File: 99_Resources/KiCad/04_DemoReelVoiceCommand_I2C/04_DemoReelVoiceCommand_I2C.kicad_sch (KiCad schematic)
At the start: 11 parts, among them J1 Conn_01x03_Pin, J4 Conn_01x03_Socket, M1 SEN0539_VoiceCommand, U1 BlueToothAudioR

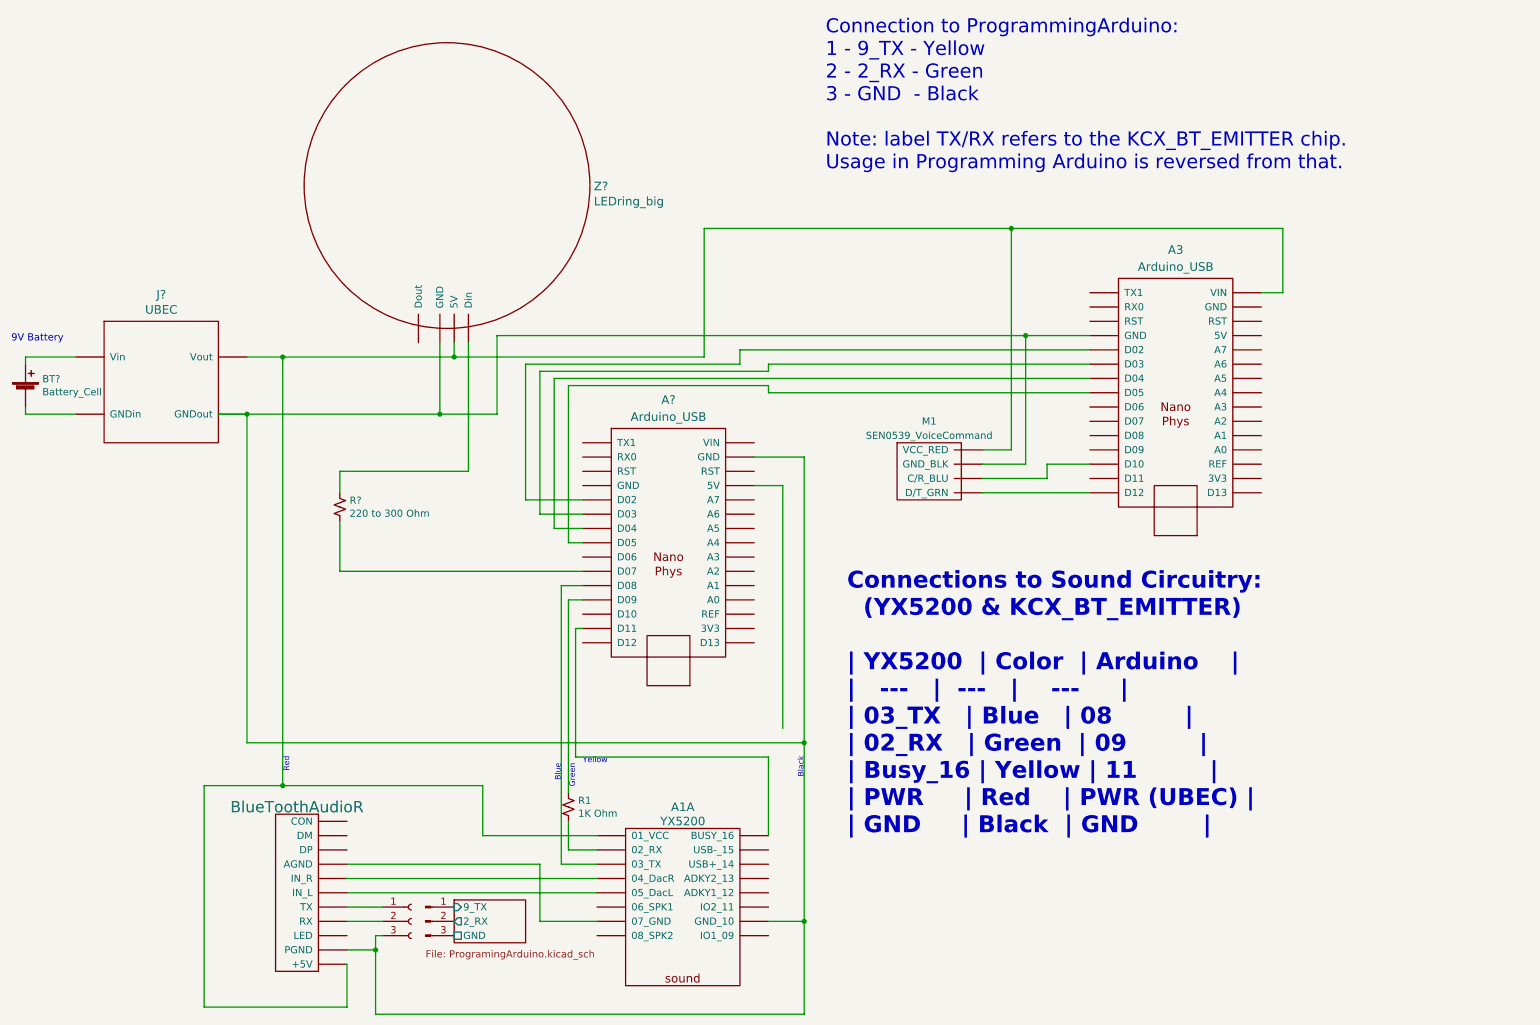
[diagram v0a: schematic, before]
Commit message: updates to UART and I2C versions of KiCad DemoReelVoiceCommand
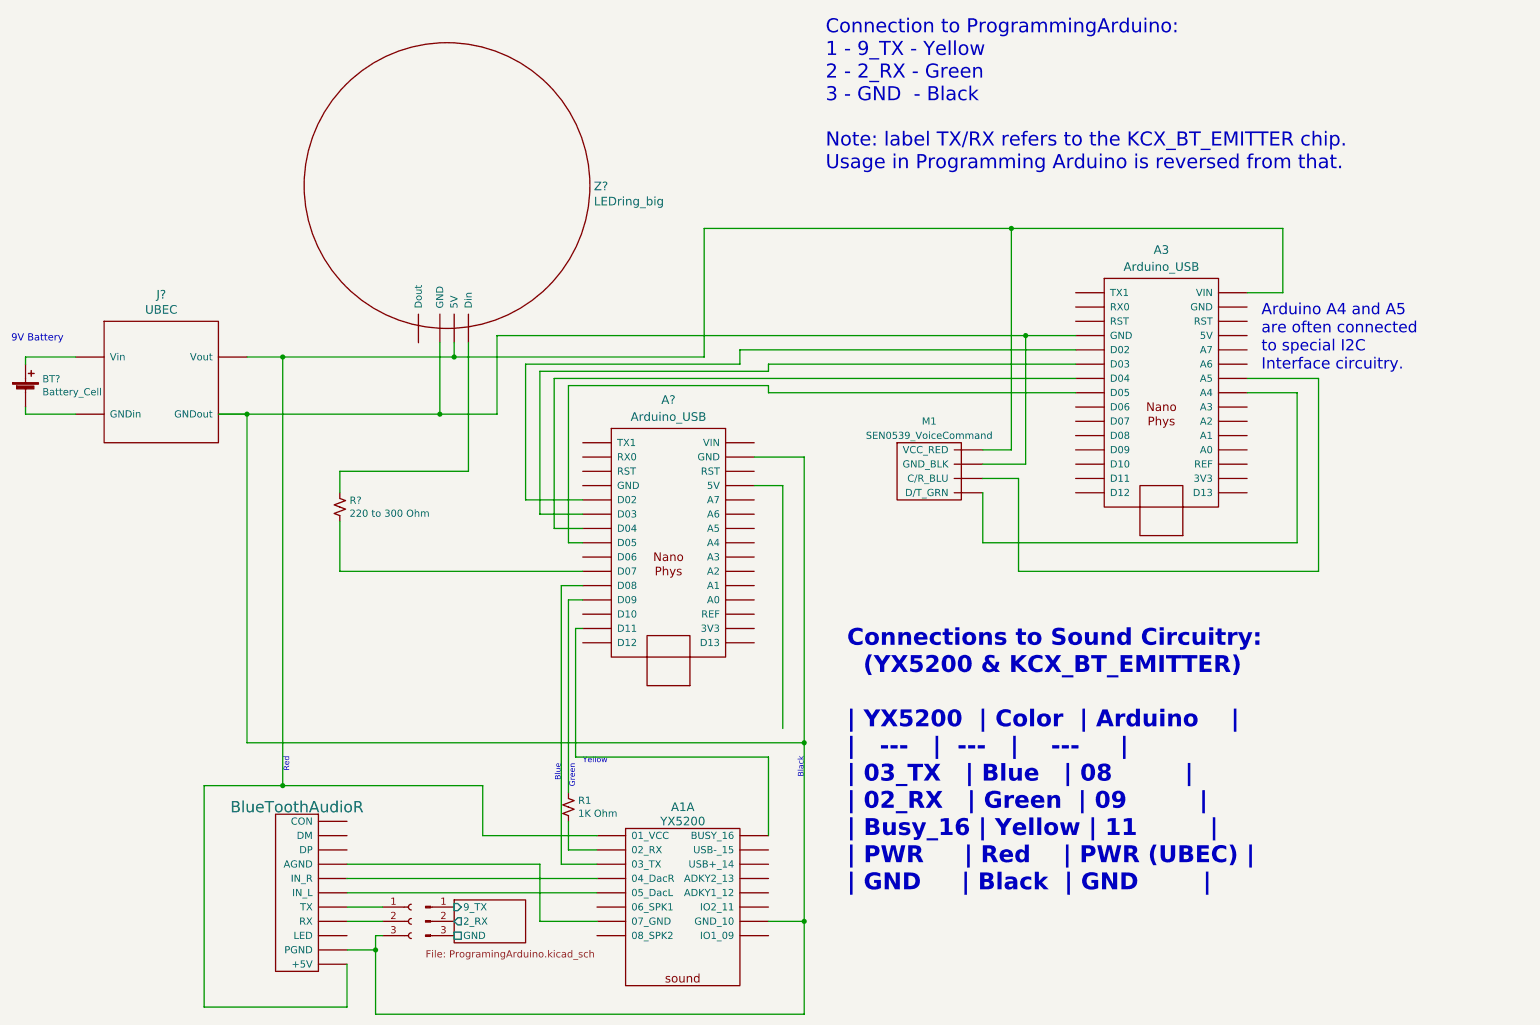
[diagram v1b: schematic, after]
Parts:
- A3, A?: symbol 04_DemoReelVoiceCommand-rescue:Arduino_USB-mdoLibrary -> 04_DemoReelVoiceCommand_I2C-rescue:Arduino_USB-mdoLibrary
- Z?: symbol 04_DemoReelVoiceCommand-rescue:LEDring_big-mdoLibrary -> 04_DemoReelVoiceCommand_I2C-rescue:LEDring_big-mdoLibrary
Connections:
- net at A?.~ (VIN): now also A3.~ (VIN)
- net at A1.~ (USB-_15): no longer A?.~ (VIN)
- net at A3.~ (VIN): no longer A?.~ (VIN)
- net at Z?.~ (GND): now also A1.~ (USB-_15), A3.~ (VIN), M1.~ (VCC_RED), U1.~ (TX)
- net at U1.~ (TX): now also J4.2 (Pin_2)
- new net: A1.~ (USB-_15), A3.~ (VIN), A?.~ (VIN), J4.3 (Pin_3), M1.~ (VCC_RED), U1.~ (TX), Z?.~ (GND)
- new net: A1.~ (USB-_15), A?.~ (VIN) (x2)
- new net: A3.~ (VIN), A?.~ (VIN) (x3)
- new net: A1.~ (USB-_15), U1.~ (TX) (x3)
- new net: A3.~ (VIN), M1.~ (VCC_RED)
- now unconnected: A1.~ (USB-_15), A1.~ (USB-_15), A1.~ (USB-_15), A1.~ (USB-_15), A1.~ (USB-_15), A1.~ (USB-_15), A3.~ (VIN), A3.~ (VIN), A3.~ (VIN), A3.~ (VIN), A3.~ (VIN), A3.~ (VIN)
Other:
- note added: "Arduino A4 and A5 are often connected to special I2C Interface circuitry."
- company: Author: https://github.com/Mark-MDO47/ArduinoClass/tree/master -> Author: https://github.com/Mark-MDO47/ArduinoClass
- title: 04 Sonar Range Detector - DemoReelVoiceCommand -> 04 The Finale - DemoReelVoiceCommand_I2C
- moved on the sheet: A3

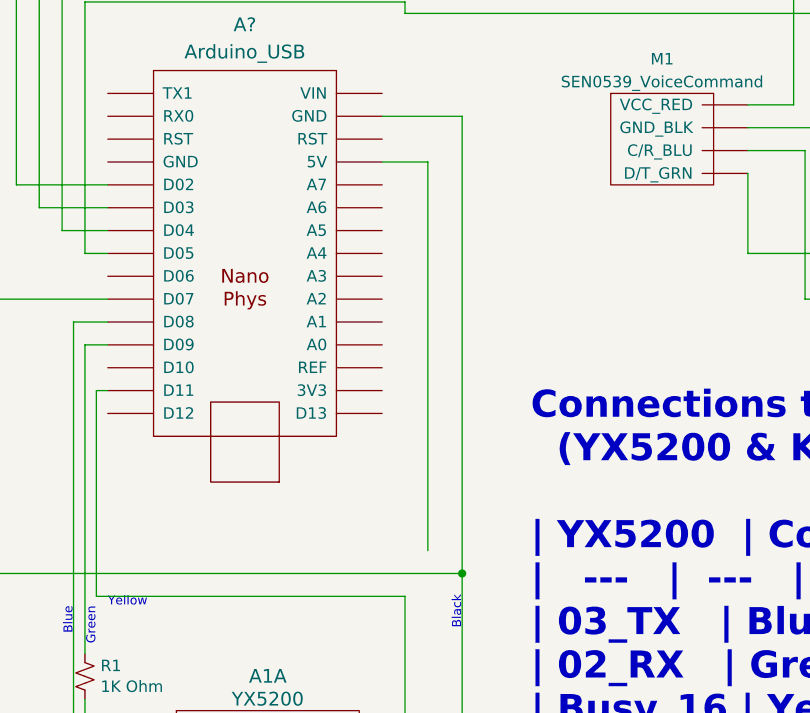
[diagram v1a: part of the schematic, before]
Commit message: more I2C
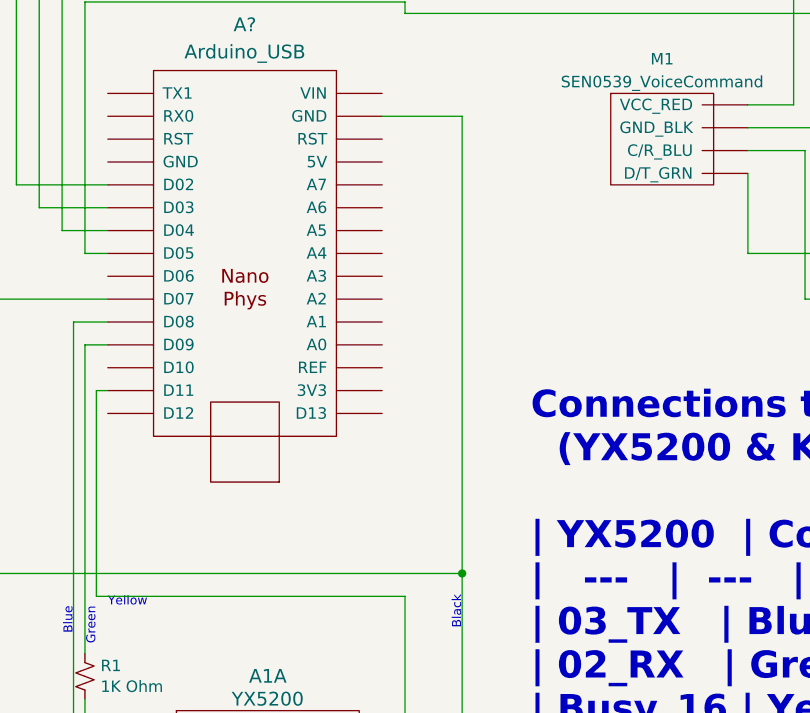
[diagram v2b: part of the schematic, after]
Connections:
- net at A?.~ (VIN): now also A3.~ (VIN)
- net at A1.~ (USB-_15): no longer A?.~ (VIN)
- net at A3.~ (VIN): no longer A?.~ (VIN)
- net at Z?.~ (GND): now also A1.~ (USB-_15), A3.~ (VIN), M1.~ (VCC_RED), U1.~ (TX)
- net at U1.~ (TX): now also J4.2 (Pin_2)
- new net: A1.~ (USB-_15), A3.~ (VIN), A?.~ (VIN), J4.3 (Pin_3), M1.~ (VCC_RED), U1.~ (TX), Z?.~ (GND)
- new net: A1.~ (USB-_15), A?.~ (VIN) (x2)
- new net: A3.~ (VIN), A?.~ (VIN) (x3)
- new net: A1.~ (USB-_15), U1.~ (TX) (x3)
- new net: A3.~ (VIN), M1.~ (VCC_RED)
- now unconnected: A1.~ (USB-_15), A1.~ (USB-_15), A1.~ (USB-_15), A1.~ (USB-_15), A1.~ (USB-_15), A1.~ (USB-_15), A3.~ (VIN), A3.~ (VIN), A3.~ (VIN), A3.~ (VIN), A3.~ (VIN), A3.~ (VIN)
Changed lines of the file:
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@@
-    (stroke (width 0) (type default))
-  )
-  (wire (pts (xy 151.13 96.52) (xy 151.13 139.7))
     (stroke (width 0) (type default))
   )
@@
     (stroke (width 0) (type default))
   )
-  (wire (pts (xy 146.05 96.52) (xy 151.13 96.52))
-    (stroke (width 0) (type default))
-  )
